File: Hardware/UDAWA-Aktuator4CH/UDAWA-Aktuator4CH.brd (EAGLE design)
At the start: 100 x 80 mm, 20 parts

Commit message: First working version of Water Sensor
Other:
- board text added: "Actuator 4Ch"
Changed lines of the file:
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@@
 https://github.com/NarinLab/Udawa</text>
 <text x="91.44" y="2.54" size="3.81" layer="21" rot="R90">UDAWA</text>
-<text x="95.25" y="2.54" size="2.54" layer="21" rot="R90">HW V.1</text>
+<text x="99.06" y="2.54" size="2.54" layer="21" rot="R90">HW V.1</text>
 <text x="74.93" y="27.94" size="2.54" layer="21" rot="R90">github.com/NarinLab/Udawa</text>
 <text x="71.12" y="27.94" size="2.54" layer="21" rot="R90">FTI Undiknas</text>
+<text x="95.25" y="2.54" size="2.54" layer="21" rot="R90">Actuator 4Ch</text>
 </plain>
 <attributes>

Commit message: PCB Print Ready
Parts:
- added RELAY_PWR: (no value), con-wago-500:W237-102
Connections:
- net 5V: now also RELAY_PWR.2
- net GND: now also RELAY_PWR.1
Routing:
- net 5V: track 67.2 -> 81.3 mm
- net GND: track 87.6 -> 98.9 mm
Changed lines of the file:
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@@
 <grid distance="50" unitdist="mil" unit="mil" style="lines" multiple="1" display="no" altdistance="5" altunitdist="mil" altunit="mil"/>
 <layers>
-<layer number="1" name="Top" color="4" fill="1" visible="yes" active="yes"/>
+<layer number="1" name="Top" color="4" fill="1" visible="no" active="yes"/>
 <layer number="16" name="Bottom" color="1" fill="1" visible="yes" active="yes"/>
 <layer number="17" name="Pads" color="2" fill="1" visible="yes" active="yes"/>
 <layer number="18" name="Vias" color="2" fill="1" visible="yes" active="yes"/>
-<layer number="19" name="Unrouted" color="6" fill="1" visible="yes" active="yes"/>
+<layer number="19" name="Unrouted" color="6" fill="1" visible="no" active="yes"/>
 <layer number="20" name="Dimension" color="24" fill="1" visible="yes" active="yes"/>
 <layer number="21" name="tPlace" color="7" fill="1" visible="yes" active="yes"/>
@@
 <layer number="27" name="tValues" color="7" fill="1" visible="yes" active="yes"/>
 <layer number="28" name="bValues" color="7" fill="1" visible="yes" active="yes"/>
-<layer number="29" name="tStop" color="7" fill="3" visible="no" active="yes"/>
-<layer number="30" name="bStop" color="7" fill="6" visible="no" active="yes"/>
-<layer number="31" name="tCream" color="7" fill="4" visible="no" active="yes"/>
-<layer number="32" name="bCream" color="7" fill="5" visible="no" active="yes"/>
-<layer number="33" name="tFinish" color="6" fill="3" visible="no" active="yes"/>
-<layer number="34" name="bFinish" color="6" fill="6" visible="no" active="yes"/>
+<layer number="29" name="tStop" color="7" fill="3" visible="yes" active="yes"/>
+<layer number="30" name="bStop" color="7" fill="6" visible="yes" active="yes"/>
+<layer number="31" name="tCream" color="7" fill="4" visible="yes" active="yes"/>
+<layer number="32" name="bCream" color="7" fill="5" visible="yes" active="yes"/>
+<layer number="33" name="tFinish" color="6" fill="3" visible="yes" active="yes"/>
+<layer number="34" name="bFinish" color="6" fill="6" visible="yes" active="yes"/>
 <layer number="35" name="tGlue" color="7" fill="4" visible="no" active="yes"/>
 <layer number="36" name="bGlue" color="7" fill="5" visible="no" active="yes"/>
 <layer number="37" name="tTest" color="7" fill="1" visible="no" active="yes"/>
 <layer number="38" name="bTest" color="7" fill="1" visible="no" active="yes"/>
-<layer number="39" name="tKeepout" color="4" fill="11" visible="yes" active="yes"/>
-<layer number="40" name="bKeepout" color="1" fill="11" visible="yes" active="yes"/>
-<layer number="41" name="tRestrict" color="4" fill="10" visible="yes" active="yes"/>
-<layer number="42" name="bRestrict" color="1" fill="10" visible="yes" active="yes"/>
-<layer number="43" name="vRestrict" color="2" fill="10" visible="yes" active="yes"/>
-<layer number="44" name="Drills" color="7" fill="1" visible="no" active="yes"/>
-<layer number="45" name="Holes" color="7" fill="1" visible="no" active="yes"/>
-<layer number="46" name="Milling" color="3" fill="1" visible="no" active="yes"/>
-<layer number="47" name="Measures" color="7" fill="1" visible="no" active="yes"/>
+<layer number="39" name="tKeepout" color="4" fill="11" visible="no" active="yes"/>
+<layer number="40" name="bKeepout" color="1" fill="11" visible="no" active="yes"/>
+<layer number="41" name="tRestrict" color="4" fill="10" visible="no" active="yes"/>
+<layer number="42" name="bRestrict" color="1" fill="10" visible="no" active="yes"/>
+<layer number="43" name="vRestrict" color="2" fill="10" visible="no" active="yes"/>
+<layer number="44" name="Drills" color="7" fill="1" visible="yes" active="yes"/>
+<layer number="45" name="Holes" color="7" fill="1" visible="yes" active="yes"/>
+<layer number="46" name="Milling" color="3" fill="1" visible="yes" active="yes"/>
+<layer number="47" name="Measures" color="7" fill="1" visible="yes" active="yes"/>
 <layer number="48" name="Document" color="7" fill="1" visible="yes" active="yes"/>
 <layer number="49" name="Reference" color="7" fill="1" visible="yes" active="yes"/>
@@
 <wire x1="100" y1="80" x2="0" y2="80" width="0" layer="20"/>
 <wire x1="0" y1="80" x2="0" y2="0" width="0" layer="20"/>
-<text x="13.97" y="1.27" size="1.27" layer="21">UDAWA Board HW Ver. 1
+<text x="2.54" y="2.54" size="1.27" layer="21">UDAWA Board HW Ver. 1
 Universal Digital Agriculture Watering Assistant
 https://github.com/NarinLab/Udawa</text>
-<text x="91.44" y="2.54" size="3.81" layer="21" rot="R90">UDAWA</text>
-<text x="99.06" y="2.54" size="2.54" layer="21" rot="R90">HW V.1</text>
+<text x="90.17" y="2.54" size="3.81" layer="21" rot="R90">UDAWA</text>
+<text x="97.79" y="2.54" size="2.54" layer="21" rot="R90">HW V.1</text>
 <text x="74.93" y="27.94" size="2.54" layer="21" rot="R90">github.com/NarinLab/Udawa</text>
 <text x="71.12" y="27.94" size="2.54" layer="21" rot="R90">FTI Undiknas</text>
-<text x="95.25" y="2.54" size="2.54" layer="21" rot="R90">Actuator 4Ch</text>
+<text x="93.98" y="2.54" size="2.54" layer="21" rot="R90">Actuator 4Ch</text>
+<hole x="68.58" y="69.85" drill="1.27"/>
+<hole x="27.94" y="12.7" drill="1.27"/>
 </plain>
 <attributes>
@@
 <attribute name="VALUE" x="5.08" y="17.74" size="1.27" layer="27" ratio="10" rot="R270"/>
 </element>
+<element name="RELAY_PWR" library="con-wago-500" package="W237-102" package3d_urn="urn:adsk.eagle:package:10688/1" value="" x="92.71" y="71.12" smashed="yes" rot="R90">
+<attribute name="MF" value="" x="82.55" y="59.69" size="1.778" layer="27" rot="R90" display="off"/>
+<attribute name="MPN" value="237-102" x="82.55" y="59.69" size="1.778" layer="27" rot="R90" display="off"/>
+<attribute name="NAME" x="97.7138" y="67.2738" size="1.27" layer="25" ratio="10" rot="R90"/>
+<attribute name="OC_FARNELL" value="unknown" x="82.55" y="59.69" size="1.778" layer="27" rot="R90" display="off"/>
+<attribute name="OC_NEWARK" value="70K9898" x="82.55" y="59.69" size="1.778" layer="27" rot="R90" display="off"/>
+<attribute name="POPULARITY" value="32" x="82.55" y="59.69" size="1.778" layer="27" rot="R90" display="off"/>
+<attribute name="VALUE" x="88.9" y="66.08" size="1.27" layer="27" ratio="10" rot="R90"/>
+</element>
 </elements>
 <signals>
@@
 <wire x1="98.349" y1="30.48" x2="95.849" y2="27.98" width="1.27" layer="1"/>
 <wire x1="95.849" y1="27.98" x2="93.98" y2="27.98" width="1.27" layer="1"/>
-<wire x1="84.255" y1="64.78" x2="87.64" y2="64.78" width="1.27" layer="1"/>
 <wire x1="90.17" y1="67.31" x2="96.52" y2="67.31" width="1.27" layer="1"/>
 <wire x1="96.52" y1="67.31" x2="98.349" y2="65.481" width="1.27" layer="1"/>
@@
 <vertex x="100.33" y="0"/>
 <vertex x="63.5" y="15.24"/>
-<vertex x="63.5" y="15.24"/>
 <vertex x="63.5" y="27.94"/>
 <vertex x="55.88" y="27.94"/>
 <vertex x="55.88" y="78.74"/>
 </polygon>
+<contactref element="RELAY_PWR" pad="1"/>
+<wire x1="84.255" y1="64.78" x2="87.64" y2="64.78" width="1.27" layer="1"/>
+<wire x1="84.255" y1="64.78" x2="87.6" y2="64.78" width="1.27" layer="1"/>
+<wire x1="91.44" y1="68.62" x2="93.98" y2="68.62" width="1.27" layer="1"/>
+<wire x1="91.44" y1="68.62" x2="87.6" y2="64.78" width="1.27" layer="1"/>
 </signal>
 <signal name="5V">
@@
 <wire x1="80.01" y1="8.27" x2="83.28" y2="5" width="1.27" layer="1"/>
 <wire x1="80.01" y1="66.04" x2="80.01" y2="8.27" width="1.27" layer="1"/>
+<contactref element="RELAY_PWR" pad="2"/>
+<wire x1="84.255" y1="67.32" x2="84.255" y2="70.285" width="1.27" layer="1"/>
+<wire x1="84.255" y1="70.285" x2="87.63" y2="73.66" width="1.27" layer="1"/>
+<wire x1="87.63" y1="73.66" x2="93.94" y2="73.66" width="1.27" layer="1"/>
+<wire x1="93.94" y1="73.66" x2="93.98" y2="73.62" width="1.27" layer="1"/>
 </signal>
 <signal name="AC1">

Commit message: Revisi terminal catu daya. Solar panel support.
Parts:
- added MCU_PWR_IN, PSU_5V: (no value), con-wago-500:W237-102
- renumbered MAIN_IN to LOAD_IN
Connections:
- net VCC renamed 3V3
- removed net GND2: U$1.GND@2
- new net VIN: MCU_PWR_IN.2, U$1.VIN
- net 5V: now also PSU_5V.2; no longer U$1.VIN
- net GND: now also MCU_PWR_IN.1, PSU_5V.1, U$1.GND@2
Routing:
- net GND: track 98.9 -> 192.4 mm
- net VIN: track 0.00 -> 64.4 mm
- net 5V: track 81.3 -> 103.0 mm
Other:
- board text added: "5V"
- board text added: "C1"
- board text added: "C2"
- board text added: "C3"
- board text added: "C4"
- board text added: "CH1"
- board text added: "CH2"
- board text added: "CH3"
- board text added: "CH4"
- board text added: "G"
- board text added: "GND"
- board text added: "L+"
- board text added: "L-"
- board text added: "LOAD IN"
- board text added: "NORC1"
- board text added: "NORC2"
- board text added: "NORC3"
- board text added: "NORC4"
- board text added: "VIN5V"
- board text added: "~ 220V IN"

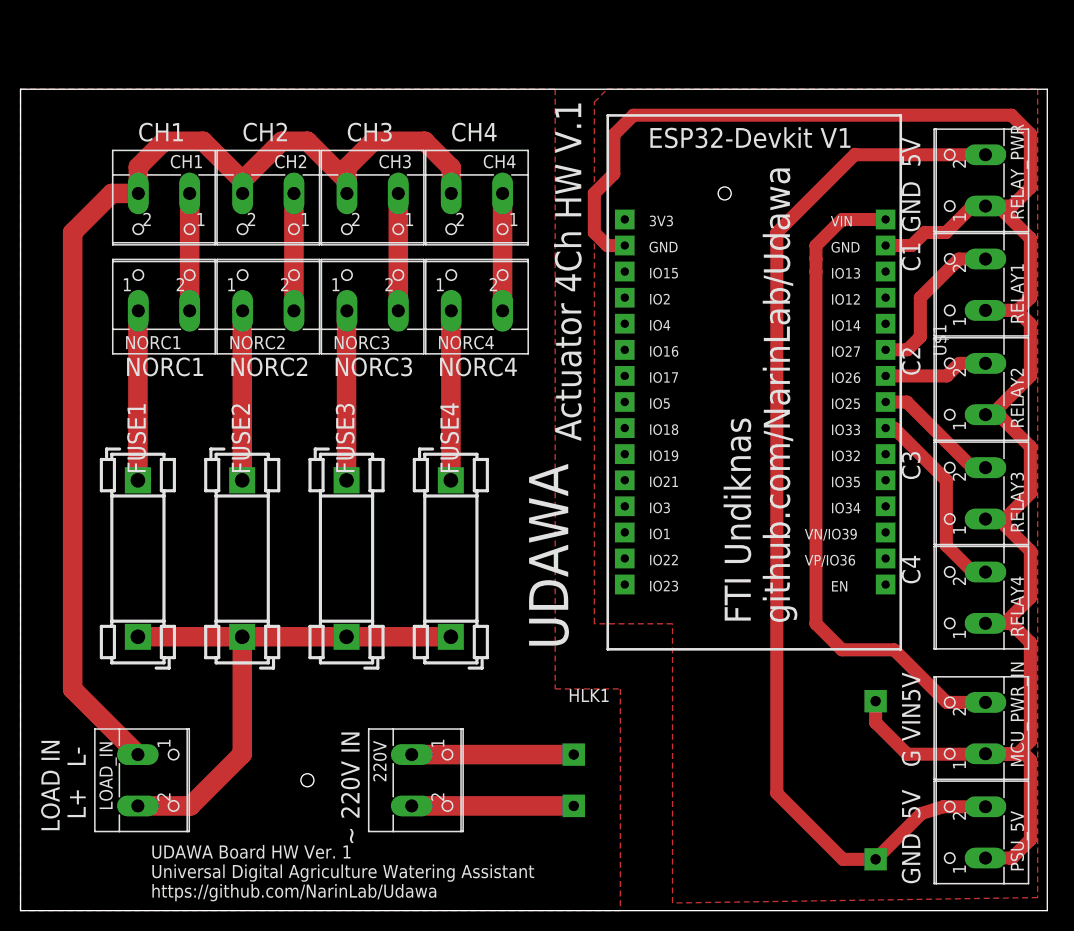
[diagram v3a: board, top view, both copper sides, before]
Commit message: revisi fuse holder ke SH22,5A (Version 1)
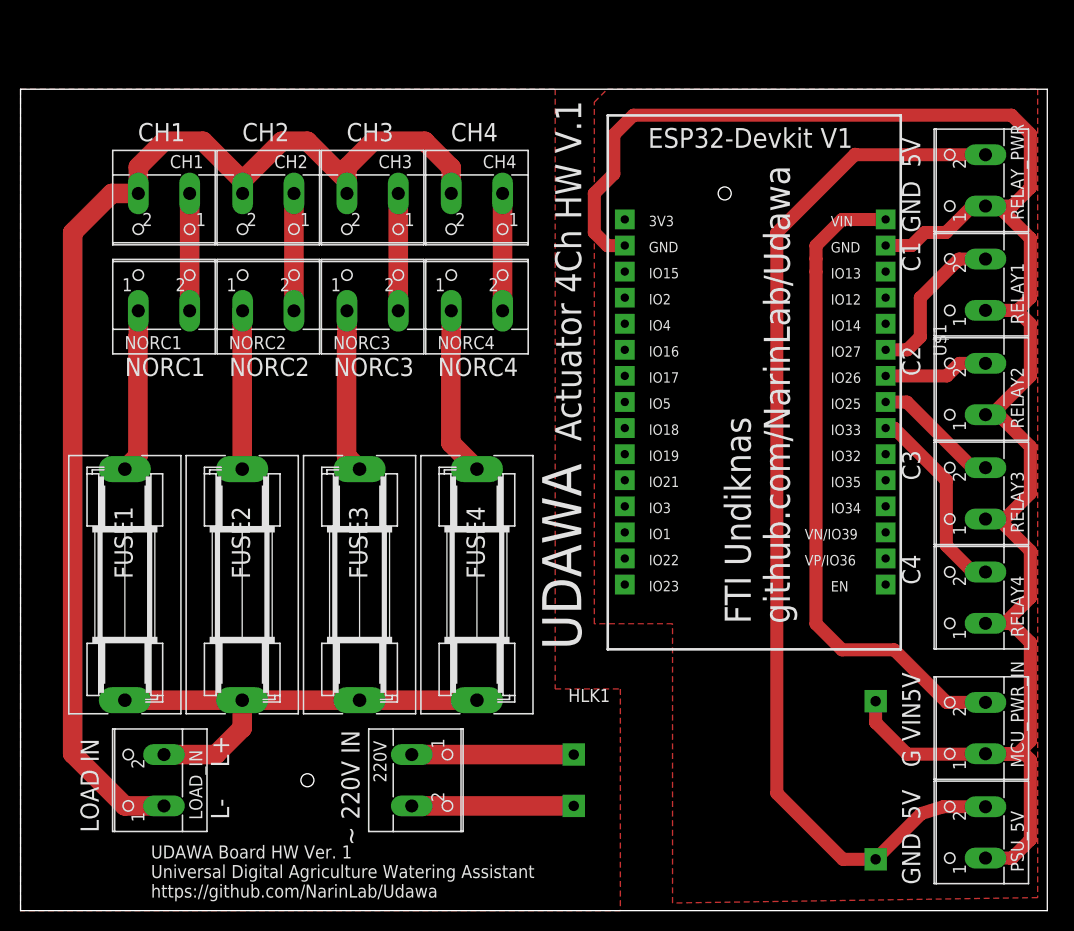
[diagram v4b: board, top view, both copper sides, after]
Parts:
- FUSE1, FUSE2, FUSE3, FUSE4: value FUSEBLANK_5X20MM -> (none); device fuse:FUSE_HOLDER_5X20MM -> fuse:SH22,5A
- moved FUSE4 10.5 mm to (44.5, 31.8)
- moved FUSE1 10.2 mm to (10.2, 31.8)
- moved FUSE3 10.2 mm to (33.0, 31.8)
- moved FUSE2 10.2 mm to (21.6, 31.8)
- turned LOAD_IN to 90 degrees
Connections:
- net M+ renamed LOAD+
- net M- renamed LOAD-
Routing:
- net LOAD+: track 54.2 -> 45.7 mm
- net LOAD-: track 109.9 -> 118.2 mm
- net F2: track 16.5 -> 15.4 mm
- net F3: track 16.5 -> 16.0 mm
- net F1: track 16.5 -> 16.0 mm
